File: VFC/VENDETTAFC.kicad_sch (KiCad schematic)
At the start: 71 parts, among them IC1 MP1584EN-LF-Z, IC2 MP1584EN-LF-Z, J1 Conn_01x08_Socket, J2 Conn_01x06_Socket, J3 Conn_01x06_Socket, J4 Conn_01x03_Socket, J5 Conn_01x04_Socket, P1 USB_C_Plug_USB2.0, SW1 SW_Push, U1 STM32F722RETx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

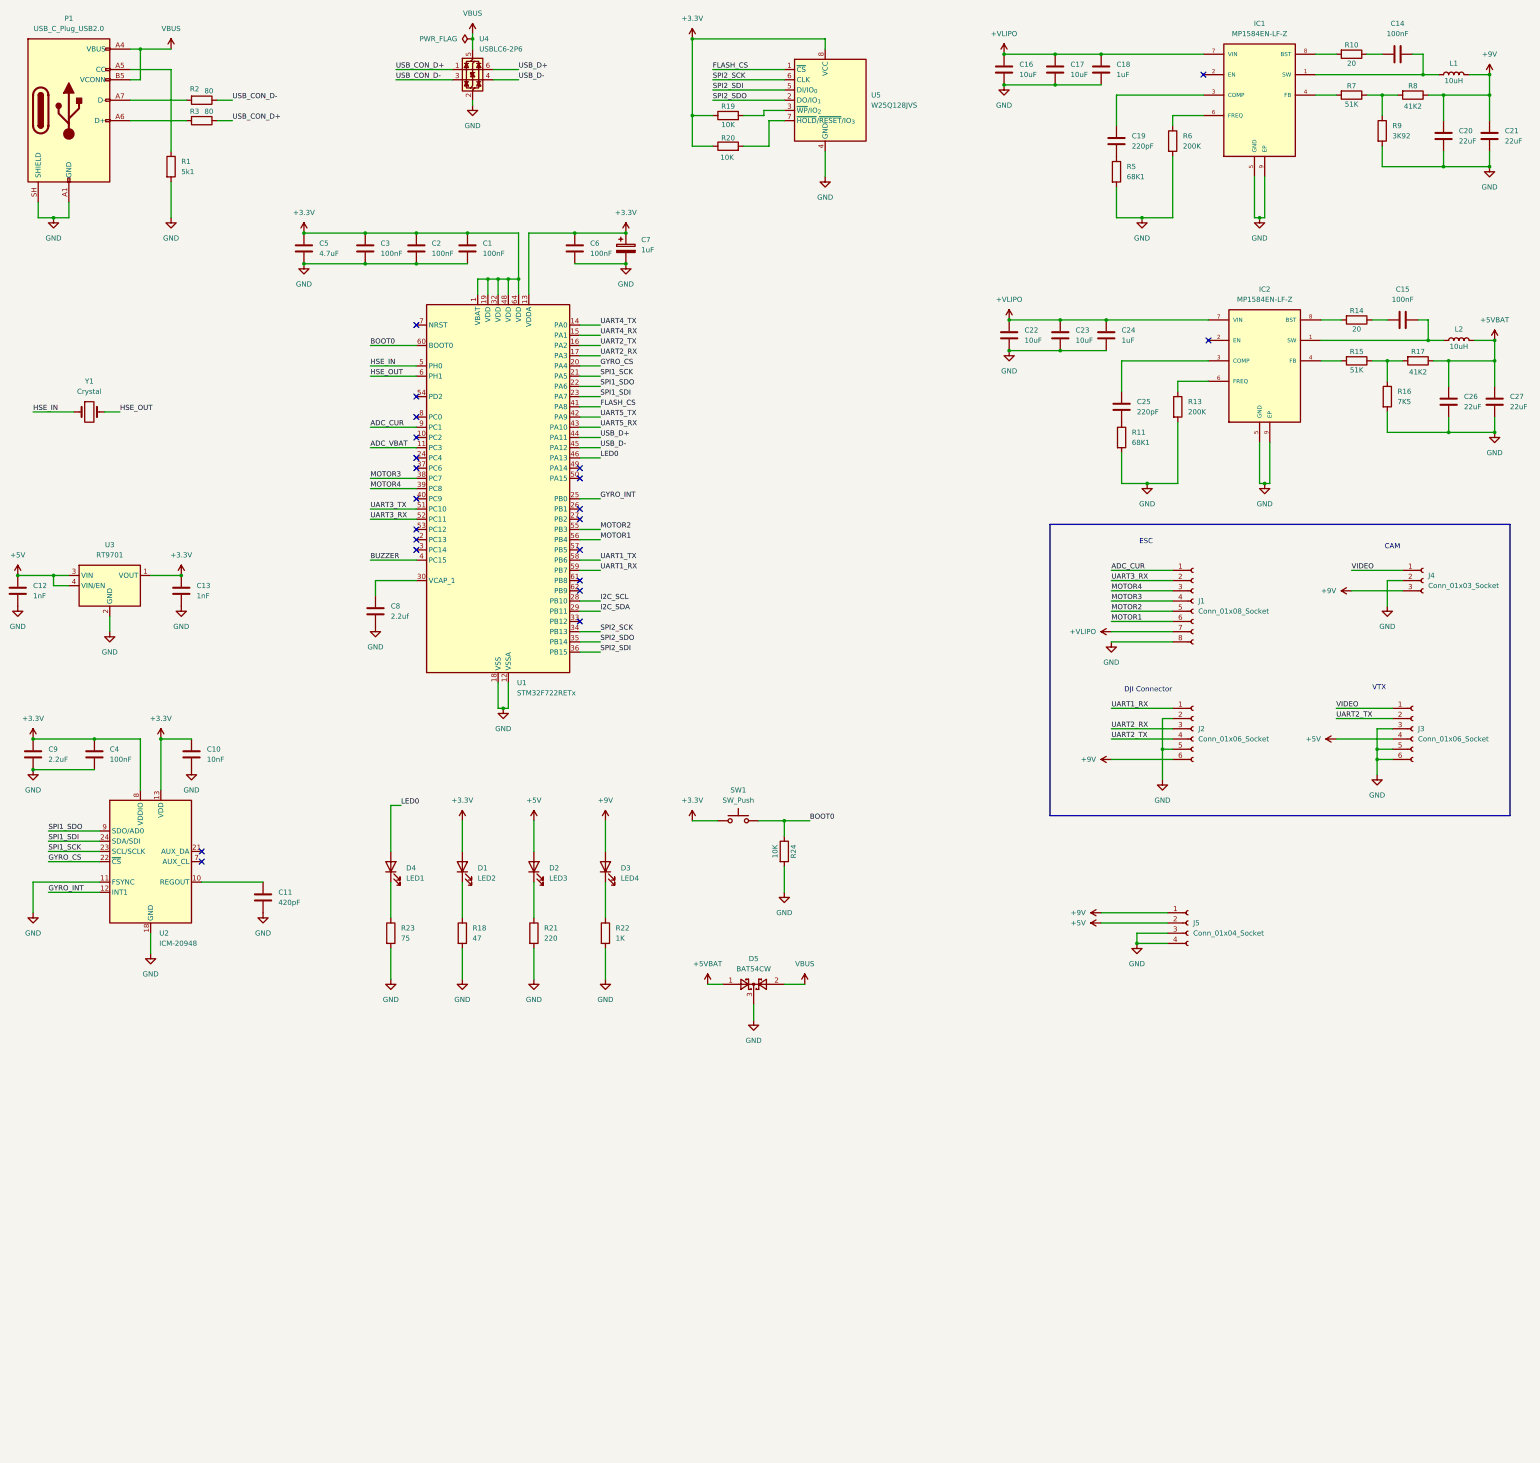
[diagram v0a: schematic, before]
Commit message: Updated VFC schematic
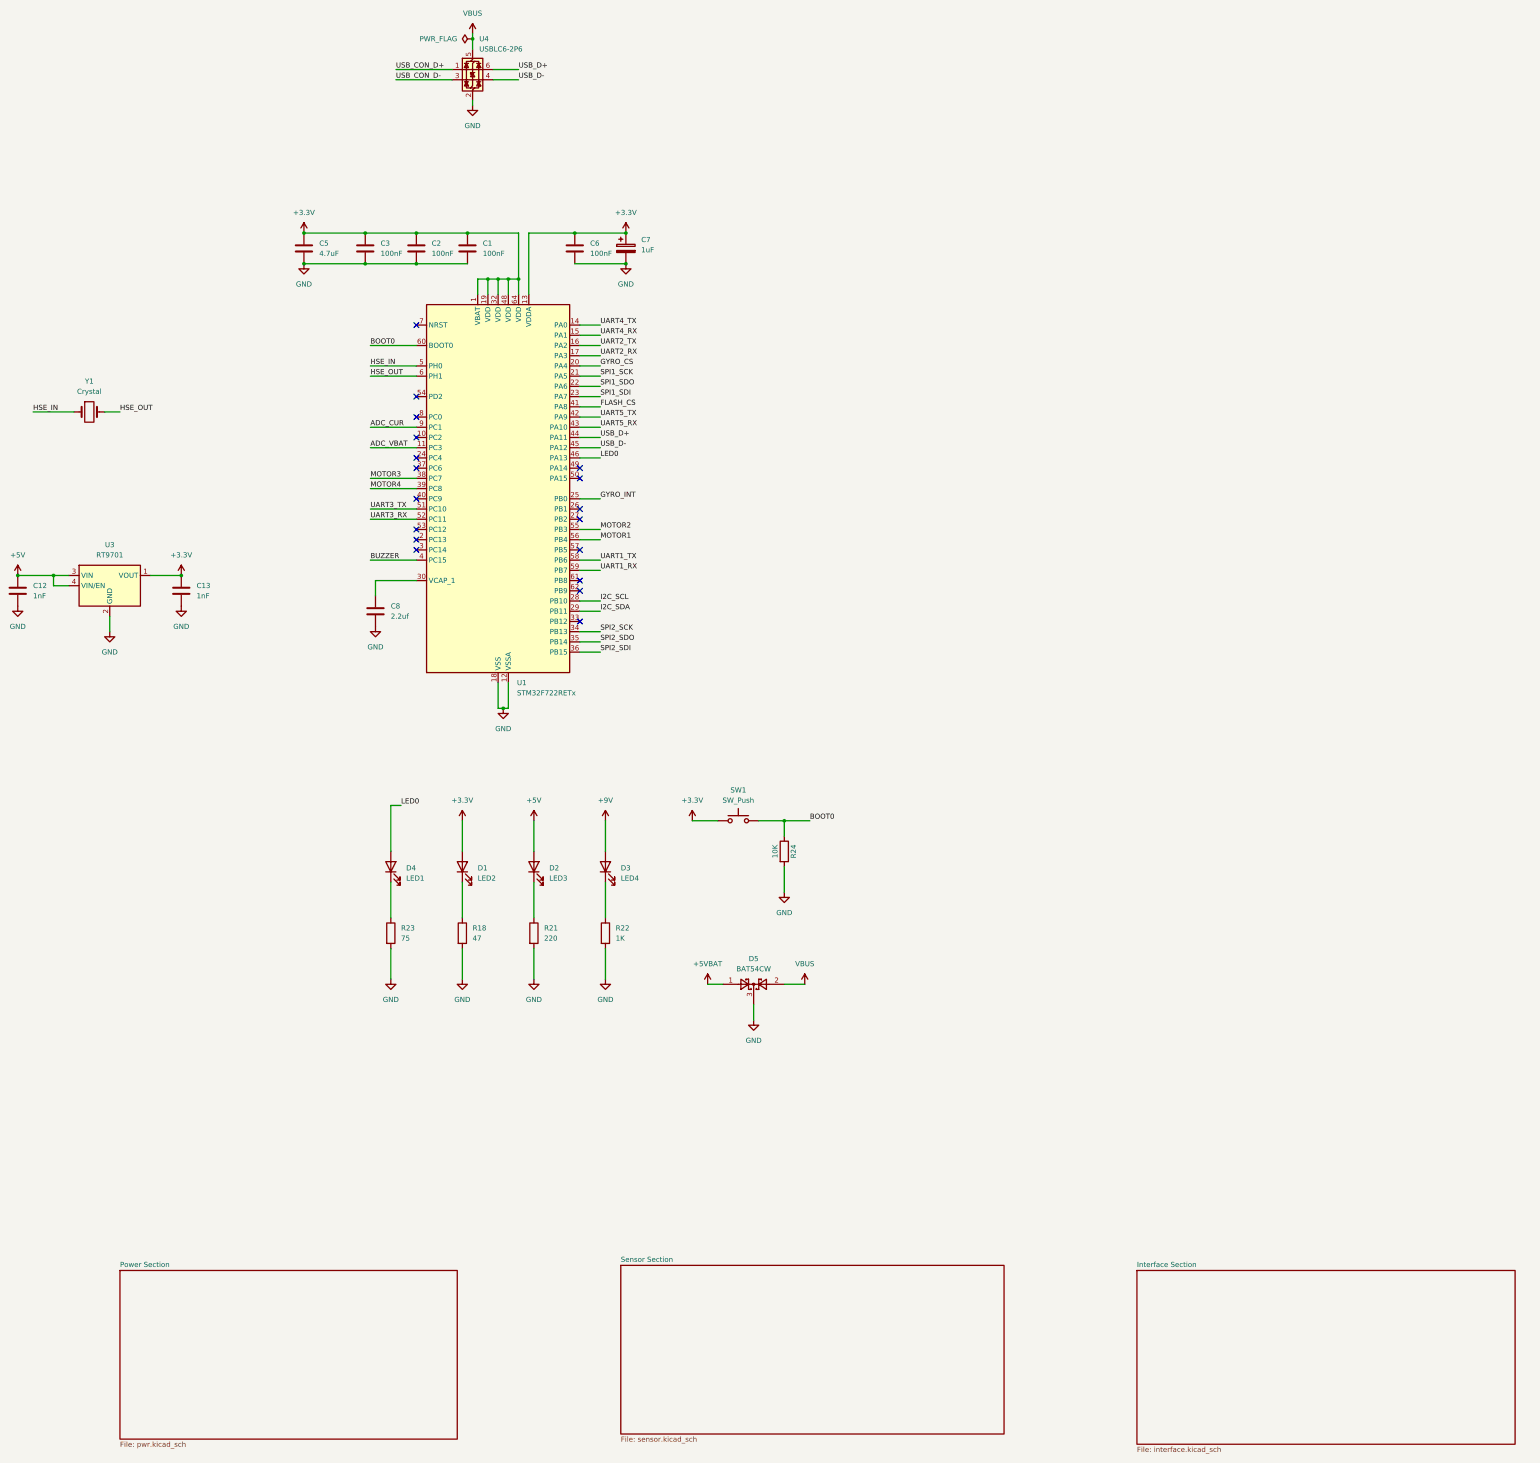
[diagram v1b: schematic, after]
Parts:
- removed C10: 10nF, Capacitor_SMD:C_0402_1005Metric, symbol Device:C
- removed C11: 420pF, Capacitor_SMD:C_0402_1005Metric, symbol Device:C
- removed C14, C15, C4: 100nF, Capacitor_SMD:C_0402_1005Metric, symbol Device:C
- removed C16, C17, C22, C23: 10uF, Capacitor_SMD:C_0402_1005Metric, symbol Device:C
- removed C18, C24: 1uF, Capacitor_SMD:C_0402_1005Metric, symbol Device:C
- removed C19, C25: 220pF, Capacitor_SMD:C_0402_1005Metric, symbol Device:C
- removed C20, C21, C26, C27: 22uF, Capacitor_SMD:C_0402_1005Metric, symbol Device:C
- removed C9: 2.2uF, Capacitor_SMD:C_0402_1005Metric, symbol Device:C
- removed IC1, IC2: MP1584EN-LF-Z, MP1584EN-LF-Z:SOIC127P600X170-9N, symbol MP1584EN-LF-Z:MP1584EN-LF-Z
- removed J1: Conn_01x08_Socket, Connector_JST:JST_SH_SM08B-SRSS-TB_1x08-1MP_P1.00mm_Horizontal, symbol Connector:Conn_01x08_Socket
- removed J2, J3: Conn_01x06_Socket, Connector_JST:JST_SH_SM06B-SRSS-TB_1x06-1MP_P1.00mm_Horizontal, symbol Connector:Conn_01x06_Socket
- removed J4: Conn_01x03_Socket, Connector_JST:JST_SH_SM03B-SRSS-TB_1x03-1MP_P1.00mm_Horizontal, symbol Connector:Conn_01x03_Socket
- removed J5: Conn_01x04_Socket, symbol Connector:Conn_01x04_Socket
- removed L1, L2: 10uH, Inductor_SMD:L_0402_1005Metric, symbol Device:L
- removed P1: USB_C_Plug_USB2.0, Connector_USB:USB_C_Receptacle_HRO_TYPE-C-31-M-12, symbol Connector:USB_C_Plug_USB2.0
- removed R1: 5k1, Resistor_SMD:R_0402_1005Metric, symbol Device:R
- removed R10, R14: 20, Resistor_SMD:R_0402_1005Metric, symbol Device:R
- removed R11, R5: 68K1, Resistor_SMD:R_0402_1005Metric, symbol Device:R
- removed R13, R6: 200K, Resistor_SMD:R_0402_1005Metric, symbol Device:R
- removed R15, R7: 51K, Resistor_SMD:R_0402_1005Metric, symbol Device:R
- removed R16: 7K5, Resistor_SMD:R_0402_1005Metric, symbol Device:R
- removed R17, R8: 41K2, Resistor_SMD:R_0402_1005Metric, symbol Device:R
- removed R19, R20: 10K, Resistor_SMD:R_0402_1005Metric, symbol Device:R
- removed R2, R3: 80, Resistor_SMD:R_0402_1005Metric, symbol Device:R
- removed R9: 3K92, Resistor_SMD:R_0402_1005Metric, symbol Device:R
- removed U2: ICM-20948, Sensor_Motion:InvenSense_QFN-24_3x3mm_P0.4mm, symbol Sensor_Motion:ICM-20948
- removed U5: W25Q128JVS, Package_SO:SOIC-8_5.3x5.3mm_P1.27mm, symbol Memory_Flash:W25Q128JVS
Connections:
- no-connect marks 22 -> 18
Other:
- added sheet Interface Section (interface.kicad_sch)
- added sheet Power Section (pwr.kicad_sch)
- added sheet Sensor Section (sensor.kicad_sch)
- note removed: "CAM"
- note removed: "DJI Connector"
- note removed: "ESC"
- note removed: "VTX"

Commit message: VFC PCB components placements complete
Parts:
- removed C12, C13: 1nF, Capacitor_SMD:C_0402_1005Metric, symbol Device:C
- removed D1: LED2, LED_SMD:LED_0805_2012Metric, symbol Device:LED
- removed D2: LED3, LED_SMD:LED_0805_2012Metric, symbol Device:LED
- removed D3: LED4, LED_SMD:LED_0805_2012Metric, symbol Device:LED
- removed D4: LED1, LED_SMD:LED_0805_2012Metric, symbol Device:LED
- removed D5: BAT54CW, Package_TO_SOT_SMD:SOT-323_SC-70, symbol Diode:BAT54CW
- removed R18: 47, Resistor_SMD:R_0402_1005Metric, symbol Device:R
- removed R21: 220, Resistor_SMD:R_0402_1005Metric, symbol Device:R
- removed R22: 1K, Resistor_SMD:R_0402_1005Metric, symbol Device:R
- removed R23: 75, Resistor_SMD:R_0402_1005Metric, symbol Device:R
- removed SW1: SW_Push, Button_Switch_SMD:SW_Push_1P1T_NO_CK_KMR2, symbol Switch:SW_Push
- removed U3: RT9701, Package_TO_SOT_SMD:SOT-23-5, symbol Power_Management:RT9701
- removed U4: USBLC6-2P6, Package_TO_SOT_SMD:SOT-666, symbol Power_Protection:USBLC6-2P6
- removed Y1: Crystal, Crystal:Crystal_SMD_0603-2Pin_6.0x3.5mm, symbol Device:Crystal
- added C16, C23: 100nF, Capacitor_SMD:C_0402_1005Metric, symbol Device:C
- added FL1: 120, BLM03EB500SZ1D:BEADC0603X33N, symbol BLM03EB500SZ1D:BLM03EB500SZ1D
- added S2: EVQ-P7A01P, EVQ-P7A01P:SW_EVQ-P7A01P, symbol EVQ-P7A01P:EVQ-P7A01P
- added TP3, TP4: TestPoint, TestPoint:TestPoint_Pad_D1.0mm, symbol Connector:TestPoint
- added Y3: C3E-8.000-18-3030-X-R, C3E-8.000-18-3030-X-R:XTAL_C3E-8.000-18-3030-X-R, symbol C3E-8.000-18-3030-X-R:C3E-8.000-18-3030-X-R
- C5: footprint Capacitor_SMD:C_0402_1005Metric -> Capacitor_SMD:C_0603_1608Metric
- C7: footprint Capacitor_SMD:C_0402_1005Metric -> Capacitor_Tantalum_SMD:CP_EIA-1608-08_AVX-J
- C8: value 2.2uf -> 2.2uF
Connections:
- net +3.3V: now also C23.1, FL1.2, S2.1_1, S2.1_2; no longer U1.13 (VDDA)
- net ADC_CUR: now also U1.2 (PC13); no longer U1.9 (PC1)
- net ADC_VBAT: now also U1.9 (PC1); no longer U1.11 (PC3)
- net BOOT0: now also S2.2_1, S2.2_2
- net GND: now also C16.2, C23.2, Y3.2 (GND), Y3.4 (GND)
- net HSE_IN: now also Y3.1
- net HSE_OUT: now also Y3.3
- net UART3_RX: now also U1.54 (PD2); no longer U1.52 (PC11)
- net UART3_TX: now also U1.53 (PC12); no longer U1.51 (PC10)
- net UART4_RX: now also U1.52 (PC11); no longer U1.15 (PA1)
- net UART4_TX: now also U1.51 (PC10); no longer U1.14 (PA0)
- net UART5_RX: now also U1.15 (PA1); no longer U1.43 (PA10)
- net UART5_TX: now also U1.14 (PA0); no longer U1.42 (PA9)
- net USB_D+: now also U1.45 (PA12); no longer U1.44 (PA11)
- net USB_D-: now also U1.44 (PA11); no longer U1.45 (PA12)
- net ESC_RX: now reaches U1.24 (PC4)
- net M1: now reaches U1.26 (PB1)
- net LED4: now reaches U1.3 (PC14)
- net FLS_CS: now reaches U1.33 (PB12)
- net UART7_TX: now reaches U1.37 (PC6)
- net GPS_SDA: now reaches U1.40 (PC9)
- net SWCLK: now reaches U1.49 (PA14)
- net SWCLK: now also TP4.1
- net USB_VBUS_SENSE: now reaches U1.50 (PA15)
- net IMU_MOSI: now reaches U1.57 (PB5)
- net IMU_INT: now reaches U1.61 (PB8)
- net IMU_CS: now reaches U1.62 (PB9)
- net at U1.7 (NRST): now also C16.1
- net BUZZER renamed BUZZ
- net FLASH_CS renamed GPS_SCL
- net GYRO_CS renamed LED3
- net GYRO_INT renamed M2
- net I2C_SCL renamed LED1
- net I2C_SDA renamed U_LED
- net LED0 renamed SWDIO
- net SWDIO: now also TP3.1
- net MOTOR1 renamed IMU_MISO
- net MOTOR2 renamed IMU_SCK
- net MOTOR3 renamed UART7_RX
- net MOTOR4 renamed LED2
- net SPI1_SCK renamed ESP_SCK
- net SPI1_SDI renamed ESP_MOSI
- net SPI1_SDO renamed ESP_MISO
- net SPI2_SCK renamed FLS_SCK
- net SPI2_SDI renamed FLS_MOSI
- net SPI2_SDO renamed FLS_MISO
- net UART1_RX renamed BAR_SDA
- net UART1_TX renamed BAR_SCL
- net UART2_RX renamed M3
- net UART2_TX renamed M4
- new net: FL1.1, U1.13 (VDDA)
- new net ESP_CS: U1.11 (PC3)
- new net UART6_RX: U1.43 (PA10)
- new net UART6_TX: U1.42 (PA9)
- no-connect marks 18 -> 3
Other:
- note added: "MCU"
- moved on the sheet: C1, C2, C3, C5, C6, C7, C8, R24, U1

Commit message: VFC PCB traces update
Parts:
- FL1: value 120 -> 120Ω @ 100MHz
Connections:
- net +3.3V: no longer C6.1, C7.1, FL1.2
- net ADC_CUR: now also U1.20 (PA4); no longer U1.2 (PC13)
- net LED3: now also U1.10 (PC2); no longer U1.20 (PA4)
- net M1: now also U1.16 (PA2); no longer U1.26 (PB1)
- net M2: now also U1.17 (PA3); no longer U1.25 (PB0)
- net M3: now also U1.25 (PB0); no longer U1.17 (PA3)
- net M4: now also U1.26 (PB1); no longer U1.16 (PA2)
- net U_LED: now also U1.2 (PC13); no longer U1.29 (PB11)
- new net +3.3VA: C6.1, C7.1, FL1.2
